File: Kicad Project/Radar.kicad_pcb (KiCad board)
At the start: 2 copper layers, 100 x 100 mm, 91 parts, among them J1 Conn_01x02, J2 Conn_01x02, J3 Conn_01x02, J4 Conn_01x02, J5 Conn_01x02, J6 Conn_01x02, J7 Conn_01x02, U1 GALI-1+, U10 GALI-2+, U11 BandpassFilter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

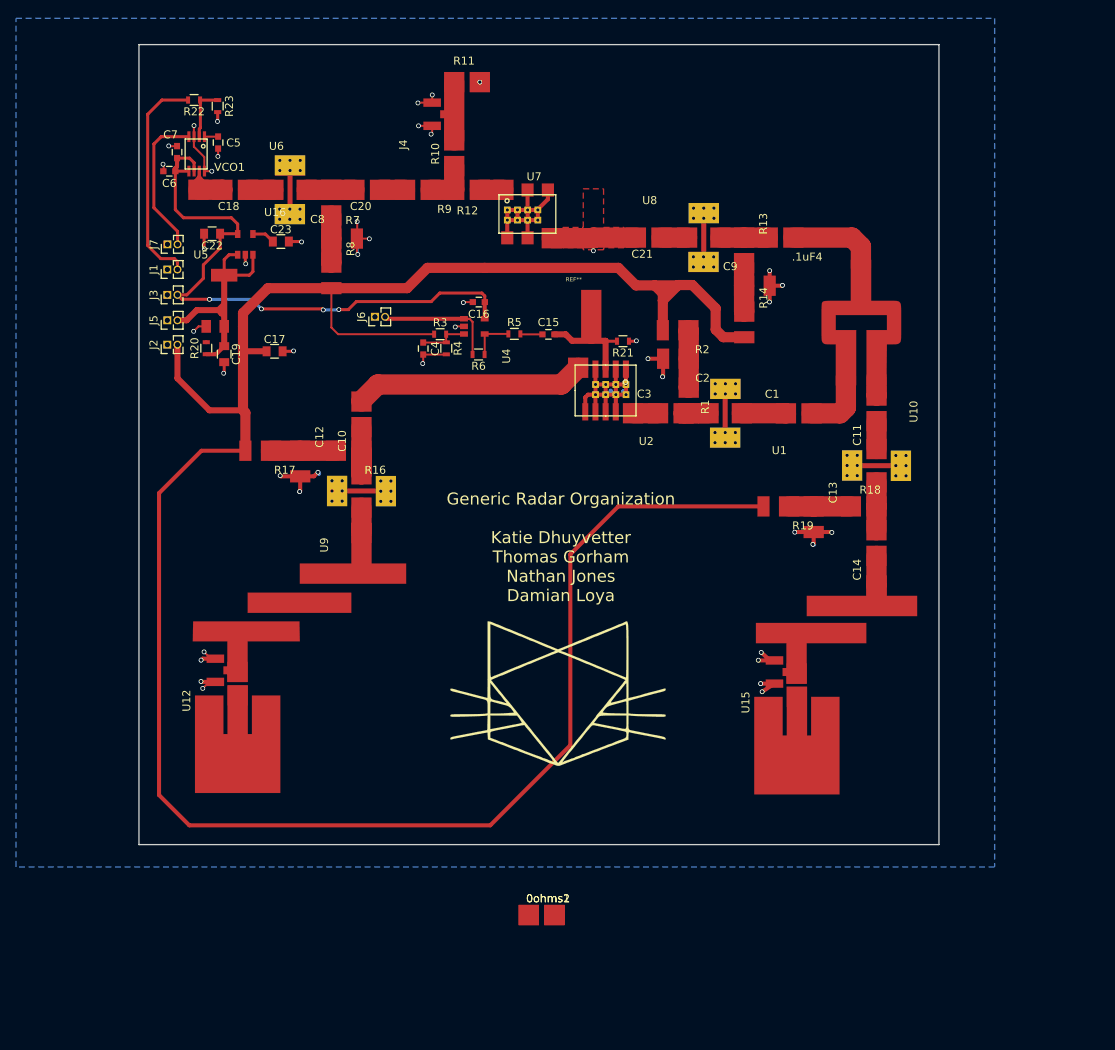
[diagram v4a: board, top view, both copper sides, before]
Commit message: Rev 2 update 1
Changes for Rev2:
Mounting Holes (duh)
Right Headers
HeadphoneJack
Added tantulum Caps at Regulators
Added UFL conns
Removed Resistive Divider
&
General layout stuff
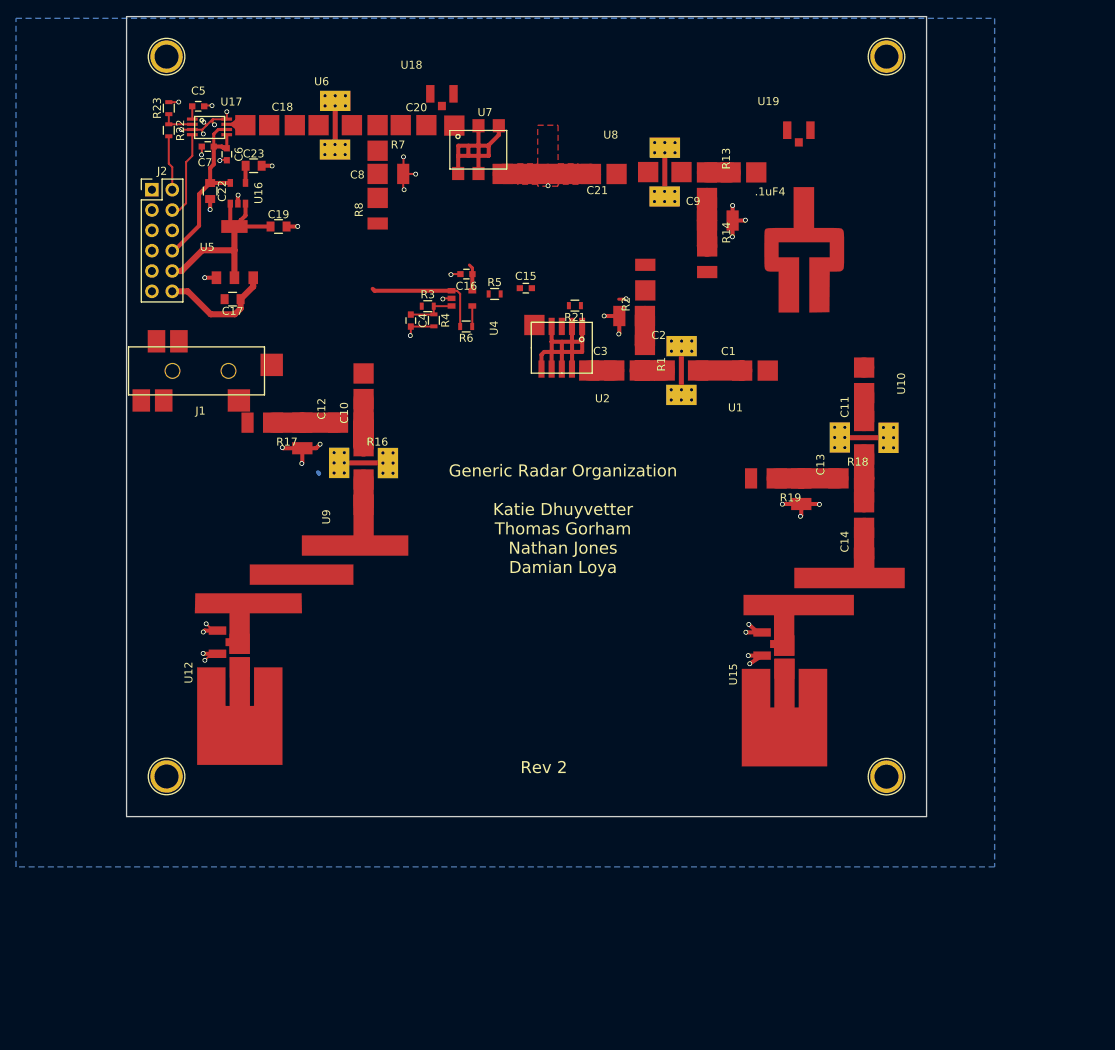
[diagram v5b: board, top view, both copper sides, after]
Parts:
- removed 0ohms1, 0ohms2, R10, R11, R12, R9: R, RadarComponents:100PAD
- removed the ? at (131.2, 77.4)
- removed the ? at (141.0, 99.2)
- removed the ? at (139.7, 99.2)
- removed the ? at (138.5, 99.2)
- removed the ? at (142.3, 97.9)
- removed the ? at (141.0, 97.9)
- removed the ? at (139.7, 97.9)
- removed the ? at (138.5, 97.9)
- removed the ? at (133.8, 137.6)
- removed the ? at (130.0, 77.4)
- removed the ? at (128.7, 77.4)
- removed the ? at (127.4, 77.4)
- removed the ? at (131.2, 76.1)
- removed the ? at (130.0, 76.1)
- removed the ? at (128.7, 76.1)
- removed the ? at (127.4, 76.1)
- removed the ? at (142.3, 99.2)
- removed J3, J5, J6, J7: Conn_01x02, Pin_Headers:Pin_Header_Straight_1x02_Pitch1.27mm
- removed J4: Conn_01x02, RadarComponents:UFL
- removed R20: R, Resistors_SMD:R_0603
- removed REF**: muwave_stub, RadarComponents:muwave_stub
- added ?: 1pin, Connectors:1pin, F.Cu at (84.8, 56.9)
- added ?: 1pin, Connectors:1pin, F.Cu at (84.8, 146.9)
- added ?: 1pin, Connectors:1pin, F.Cu at (174.8, 146.9)
- added ?: 1pin, Connectors:1pin, F.Cu at (174.8, 56.9)
- added U18: ufl, RadarComponents:UFL, F.Cu at (119.3, 61.6)
- added U19: ufl, RadarComponents:UFL, F.Cu at (163.9, 66.1)
- C19: value C -> 10uF
- J1: value Conn_01x02 -> JACK_TRS_6PINS; footprint Pin_Headers:Pin_Header_Straight_1x02_Pitch1.27mm -> RadarComponents:3.5mm_SMD
- J2: value Conn_01x02 -> CONN_02X06; footprint Pin_Headers:Pin_Header_Straight_1x02_Pitch1.27mm -> Pin_Headers:Pin_Header_Straight_2x06_Pitch2.54mm
- moved J2 19.5 mm to (83.0, 73.6), turned to 0 degrees
- moved C19 17.3 mm to (98.8, 78.2), turned to 0 degrees
- moved J1 13.2 mm to (81.1, 96.2), turned to 0 degrees
- moved MS1 11.6 mm to (163.2, 83.2)
- moved U7 10.1 mm to (120.5, 66.4)
- moved C23 10.1 mm to (95.7, 70.6)
- moved C18 9.97 mm to (99.6, 64.2)
- moved R7 9.94 mm to (109.9, 66.8)
- moved C8 9.94 mm to (112.5, 72.9)
- moved C20 9.94 mm to (116.0, 64.2)
- moved R8 9.94 mm to (110.0, 75.9)
- moved U6 9.86 mm to (105.1, 66.8)
- moved C21 9.73 mm to (139.8, 70.3)
- moved U8 9.52 mm to (146.3, 72.6)
- moved R13 9.37 mm to (151.1, 72.7)
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- renumbered VCO1 to U17
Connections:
- J1 pad 2: Net-(J1-Pad2) -> /DownconverterPreampModule/AudioOut
- J2 pad 2: +9V -> /SourceModule.sch/VCOTune
- R18 pad 2: Net-(C14-Pad2) -> Net-(R18-Pad2)
- R22 pad 2: Net-(J1-Pad2) -> /SourceModule.sch/VCOTune
- R6 pad 2: Net-(J6-Pad2) -> /DownconverterPreampModule/AudioOut
- U10 pad 3: Net-(C14-Pad2) -> Net-(R18-Pad2)
- U11 pad 1: Net-(C14-Pad1) -> Net-(R18-Pad2)
- U17 pad 4: Net-(J7-Pad2) -> /SourceModule.sch/VCOENABLE
- U4 pad 1: Net-(J6-Pad2) -> /DownconverterPreampModule/AudioOut
- U7 pad 1: Net-(R12-Pad1) -> Net-(C20-Pad1)
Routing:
- net +9V: track 306.8 -> 14.5 mm
- net +3V3: track 79.8 -> 30.3 mm, vias 4 -> 0
- net RFIN: track 28.9 -> 0.00 mm
- net Net-(J1-Pad2): track 28.1 -> 0.00 mm
- net Net-(J7-Pad2): track 18.5 -> 0.00 mm
- net +5V: track 44.6 -> 26.3 mm
- net GND: track 143.9 -> 125.5 mm, vias 44 -> 40
- net Net-(J6-Pad2): track 15.3 -> 0.00 mm
- net /DownconverterPreampModule/AudioOut: track 0.00 -> 15.3 mm
- net Net-(J4-Pad1): track 12.9 -> 0.00 mm
- net Net-(C15-Pad2): track 11.7 -> 0.00 mm
- net Net-(.1uF4-Pad1): track 11.5 -> 0.00 mm
- net /SourceModule.sch/VCOENABLE: track 0.00 -> 11.0 mm
- net PowerSplitter: track 10.8 -> 0.00 mm
- net (no net): track 0.09 -> 9.96 mm, vias 0 -> 1
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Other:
- board text added: "Rev 2"

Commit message: More Routing
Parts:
- removed C14: 100n, RadarComponents:100PAD
- moved R19 18.7 mm to (178.5, 106.5), turned to 90 degrees
- moved C13 9.42 mm to (172.1, 109.0)
- moved U4 7.37 mm to (123.3, 79.0)
- moved C4 7.37 mm to (116.8, 82.7)
- moved R3 7.37 mm to (118.9, 80.9)
- moved R6 7.37 mm to (123.7, 83.4)
- moved C15 7.37 mm to (131.1, 78.6)
- moved C16 7.37 mm to (123.7, 76.9)
- moved R4 7.37 mm to (119.6, 82.7)
- moved R5 7.37 mm to (127.2, 79.4)
- moved R17 6.67 mm to (103.6, 101.5), turned to 90 degrees
- moved C11 5.90 mm to (167.7, 95.8)
- moved U10 5.90 mm to (165.2, 101.8)
- moved U11 5.59 mm to (160.6, 127.7)
- moved U13 5.59 mm to (154.4, 141.5)
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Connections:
- J1 pad 2: /DownconverterPreampModule/AudioOut -> AudioOut
- J1 pad 3: /DownconverterPreampModule/AudioOut -> AudioOut
- J1 pad 5: /DownconverterPreampModule/AudioOut -> AudioOut
- J1 pad 6: /DownconverterPreampModule/AudioOut -> AudioOut
- J2 pad 6: /SourceModule.sch/AudioOut -> AudioOut
- R6 pad 2: /DownconverterPreampModule/AudioOut -> AudioOut
- U4 pad 1: /DownconverterPreampModule/AudioOut -> AudioOut
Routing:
- net AudioOut: track 0.00 -> 47.2 mm
- net RFIN: track 0.00 -> 18.9 mm
- net /DownconverterPreampModule/AudioOut: track 15.3 -> 0.00 mm
- net PowerSplitter: track 0.00 -> 13.9 mm
- net Net-(.1uF4-Pad1): track 0.00 -> 9.28 mm
- net Net-(R18-Pad2): track 6.00 -> 14.8 mm
- net Net-(C13-Pad2): track 7.73 -> 0.00 mm
- net Net-(C14-Pad1): track 3.72 -> 0.00 mm
- net Net-(C12-Pad2): track 8.11 -> 4.46 mm
- net Net-(U12-Pad1): track 0.00 -> 2.94 mm

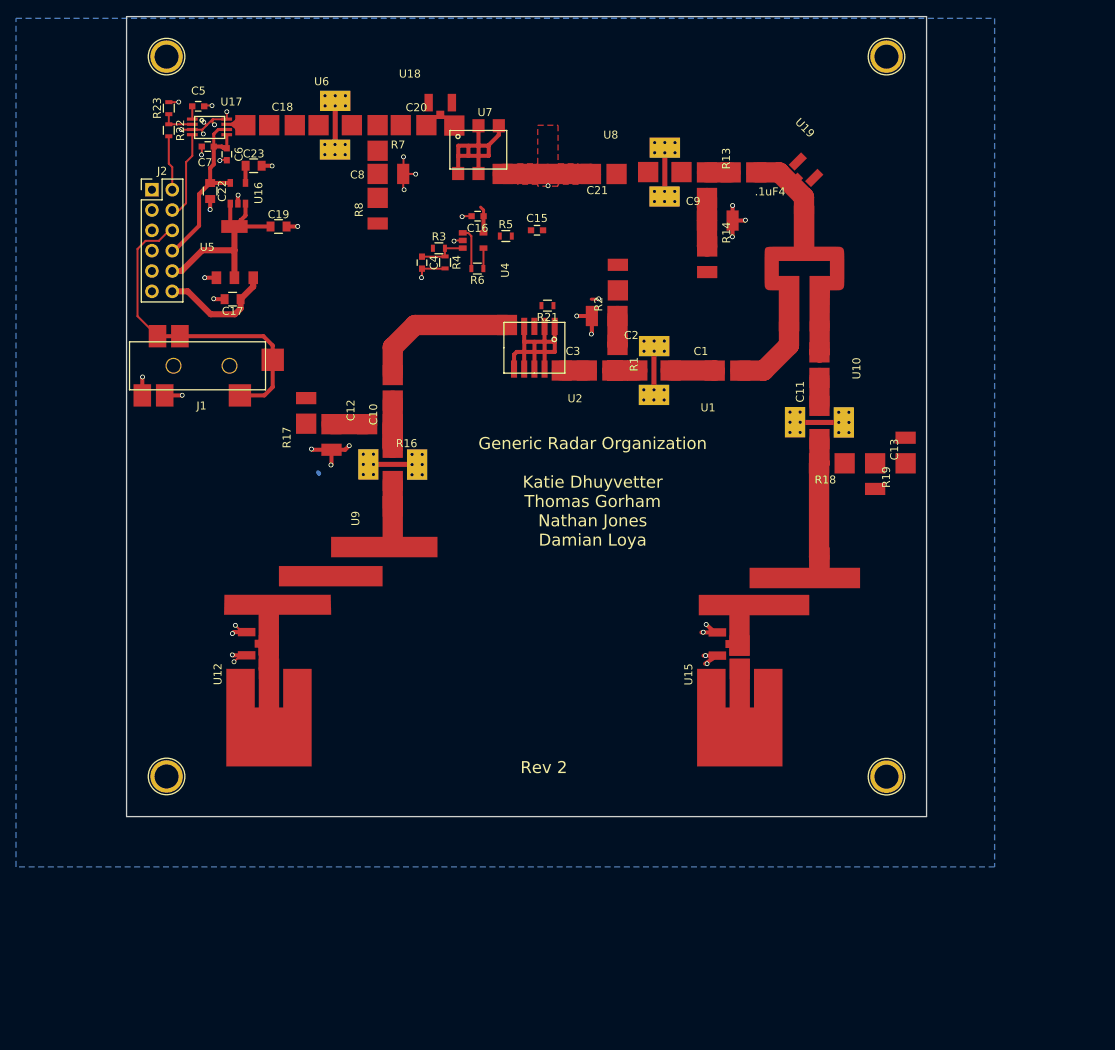
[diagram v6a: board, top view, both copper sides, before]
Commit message: Damian's almost to rev 2 completion, needs audio amps
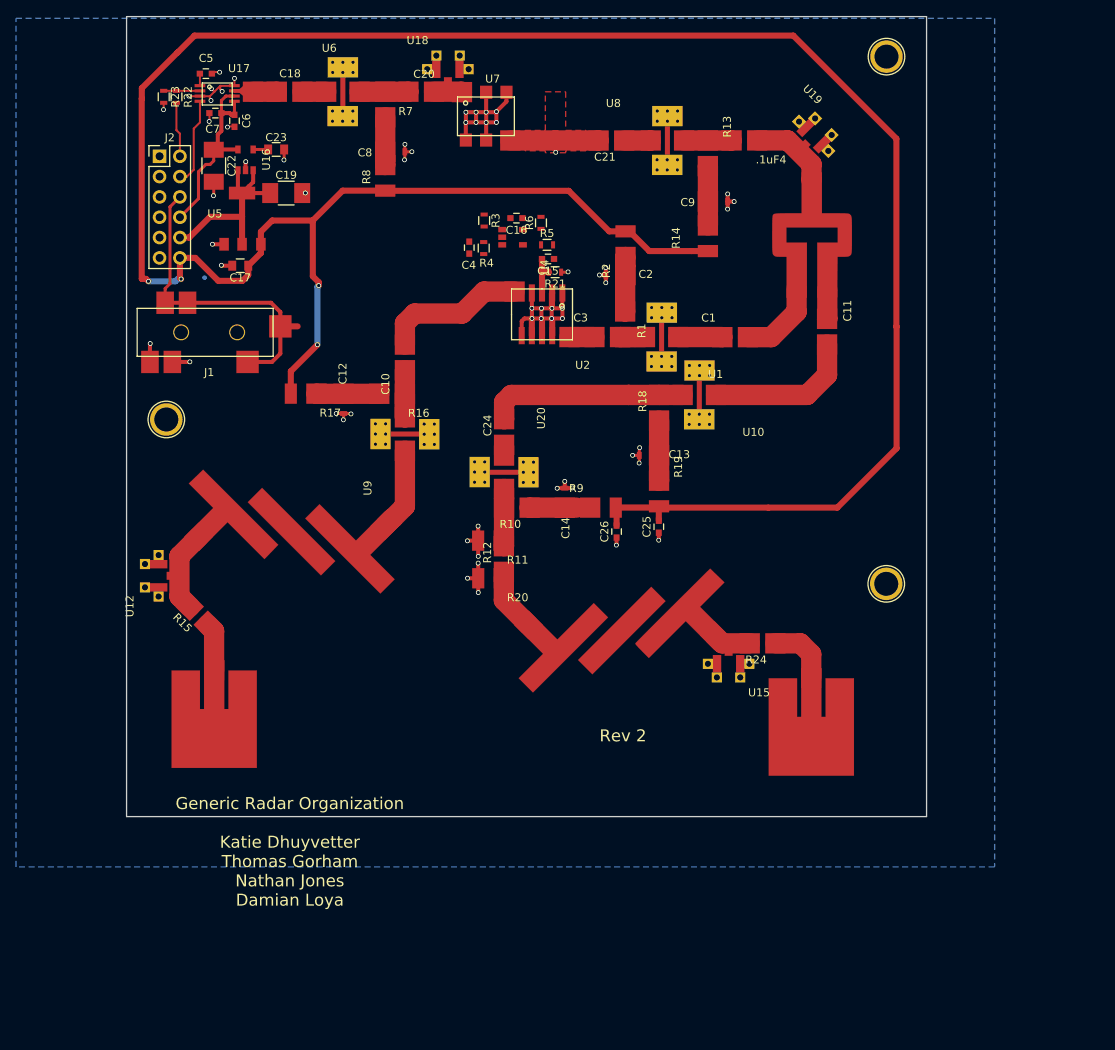
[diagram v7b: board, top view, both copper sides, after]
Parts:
- removed the ? at (84.8, 56.9)
- added C14: 100n, RadarComponents:100PAD+GND3, F.Cu at (135.9, 112.1)
- added C24: 10n, RadarComponents:100PAD, F.Cu at (128.3, 104.2)
- added C25: 1uF, Capacitors_SMD:C_0603, F.Cu at (146.4, 115.7)
- added C26: 1uF, Capacitors_SMD:C_0603, F.Cu at (141.1, 116.3)
- added R10: 75, RadarComponents:100PAD, F.Cu at (128.9, 112.0)
- added R11: R, RadarComponents:100PAD+GND2, F.Cu at (125.7, 116.2)
- added R12: R, RadarComponents:100PAD, F.Cu at (128.3, 120.1)
- added R15: R, RadarComponents:100PAD, F.Cu at (90.0, 126.2)
- added R20: R, RadarComponents:100PAD+GND2, F.Cu at (125.7, 120.9)
- added R24: R, RadarComponents:100PAD, F.Cu at (159.7, 129.0)
- added R9: 75, RadarComponents:100PAD+GND2, F.Cu at (139.1, 114.6)
- added U20: GALI-2+, RadarComponents:Amplifier, F.Cu at (125.7, 108.1)
- C11: value 100n -> 10n
- C12, C2, C8, C9: footprint RadarComponents:100PAD+GND2 -> RadarComponents:100PAD+GND3
- C13: footprint RadarComponents:100PAD+GND -> RadarComponents:100PAD+GND3
- C15: value ?F -> 1uF
- C19, C22: footprint Capacitors_SMD:C_0805 -> Capacitors_SMD:C_1210_HandSoldering
- R3: value 47k -> 10k
- U11: footprint RadarComponents:DoubleFilter -> RadarComponents:QuadPoleFilter
- U6: value GALI-2+ -> LEE-39+
- moved ? 44.6 mm to (84.8, 102.3)
- moved R19 33.7 mm to (145.1, 111.2), turned to 270 degrees
- moved C13 27.2 mm to (145.1, 105.5), turned to 180 degrees
- moved ? 24.1 mm to (174.8, 122.8)
- moved R18 21.3 mm to (147.7, 101.2), turned to 90 degrees
- moved U11 19.3 mm to (141.3, 128.5), turned to 315 degrees
- moved U12 13.9 mm to (83.8, 121.8)
- moved U10 13.5 mm to (152.2, 98.0), turned to 180 degrees
- moved R6 9.79 mm to (131.6, 77.7), turned to 90 degrees
- moved U13 9.02 mm to (163.3, 142.7)
- moved U3 7.09 mm to (100.8, 116.1), turned to 45 degrees
- moved U14 6.85 mm to (88.7, 141.7)
- moved R3 6.64 mm to (124.5, 77.4), turned to 270 degrees
- moved C4 6.20 mm to (122.7, 80.8)
- moved R5 5.27 mm to (132.4, 80.5)
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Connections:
- R18 pad 2: Net-(R18-Pad2) -> Net-(C24-Pad2)
- R3 pad 1: +9V -> +3V3
- U10 pad 3: Net-(R18-Pad2) -> Net-(C24-Pad2)
- U11 pad 1: Net-(R18-Pad2) -> Net-(R12-Pad1)
- U11 pad 2: Net-(U11-Pad2) -> Net-(R24-Pad2)
- U12 pad 1: Net-(U12-Pad1) -> Net-(R15-Pad2)
- U13 pad 1: Net-(U11-Pad2) -> Net-(R24-Pad1)
- U14 pad 1: Net-(U12-Pad1) -> Net-(R15-Pad1)
- U15 pad 1: Net-(U11-Pad2) -> Net-(R24-Pad2)
- U2 pad 2: (no net) -> GND
- U2 pad 4: (no net) -> GND
- U2 pad 6: (no net) -> GND
- U2 pad 7: (no net) -> GND
- U2 pad 8: (no net) -> GND
- U2 pad 9: (no net) -> GND
- U3 pad 1: Net-(U12-Pad1) -> Net-(R15-Pad2)
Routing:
- net +9V: track 14.5 -> 321.2 mm, vias 0 -> 4
- net Net-(C24-Pad2): track 0.00 -> 24.9 mm
- net Net-(C11-Pad1): track 3.48 -> 18.7 mm
- net Net-(R18-Pad2): track 14.8 -> 0.00 mm
- net Net-(R15-Pad2): track 0.00 -> 13.7 mm
- net Net-(C14-Pad2): track 0.00 -> 10.7 mm
- net Net-(C13-Pad2): track 0.00 -> 10.7 mm
- net (no net): track 9.96 -> 0.08 mm, vias 1 -> 0
- net Net-(R10-Pad2): track 0.00 -> 9.51 mm
- net Net-(C20-Pad2): track 0.00 -> 9.01 mm
- net Net-(R24-Pad1): track 0.00 -> 8.04 mm
- net Net-(C8-Pad2): track 0.00 -> 7.63 mm
- net Net-(R24-Pad2): track 0.00 -> 7.58 mm
- net Net-(U3-Pad2): track 3.16 -> 10.5 mm
- net Net-(R12-Pad1): track 0.00 -> 7.12 mm
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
